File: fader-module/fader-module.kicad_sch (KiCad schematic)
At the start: 26 parts, among them IC1 LMD18245T_NOPB, J4 Conn_01x05_Pin, J5 Conn_01x05_Pin, SW1 1825910-6, SW2 1825910-6, U5 ATMEGA328P-AUR

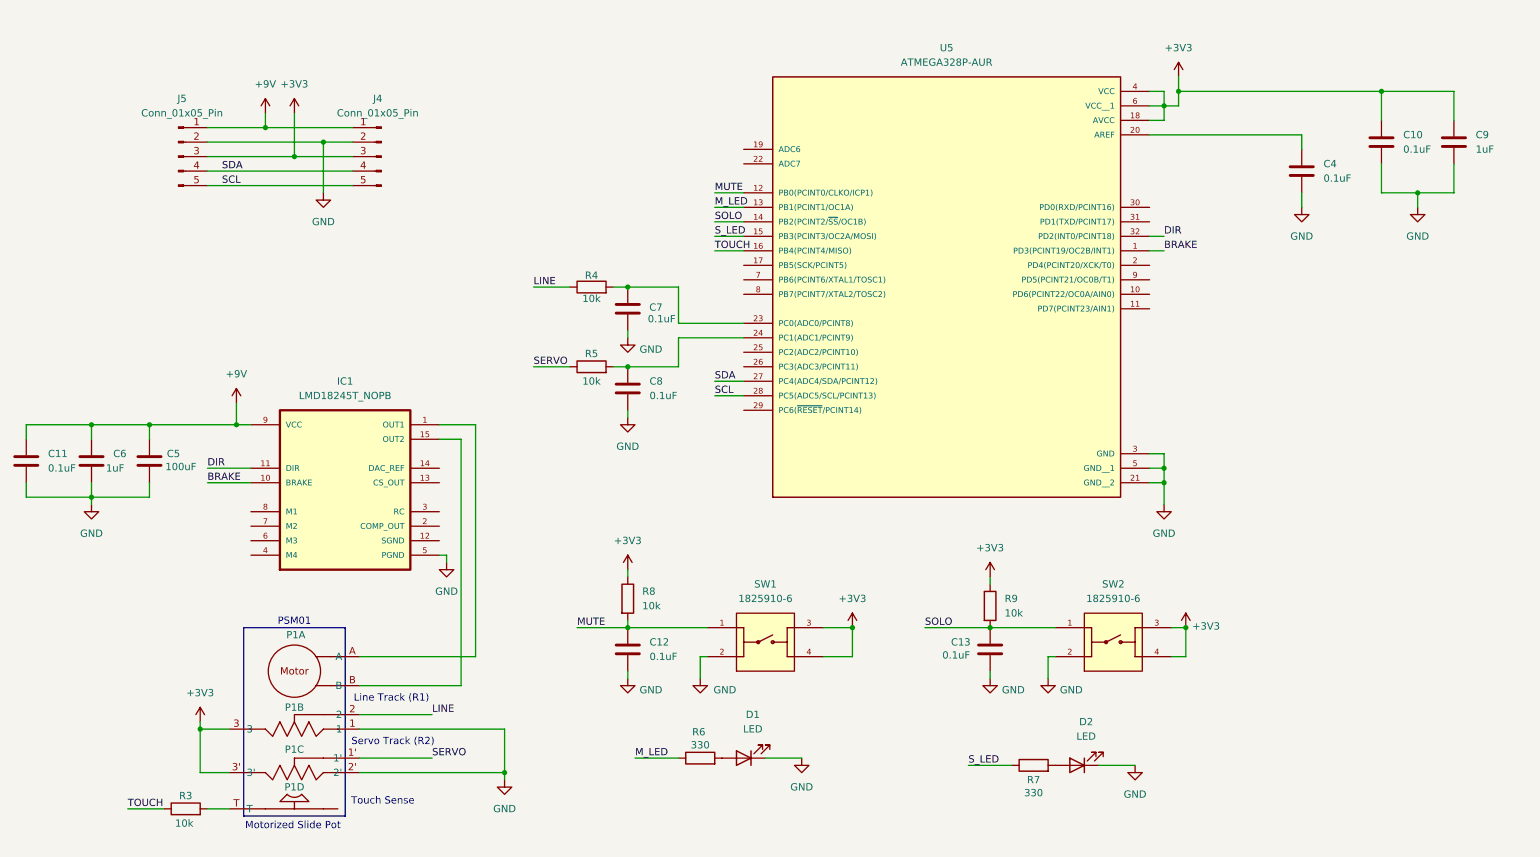
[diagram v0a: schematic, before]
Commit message: move fader module to new project
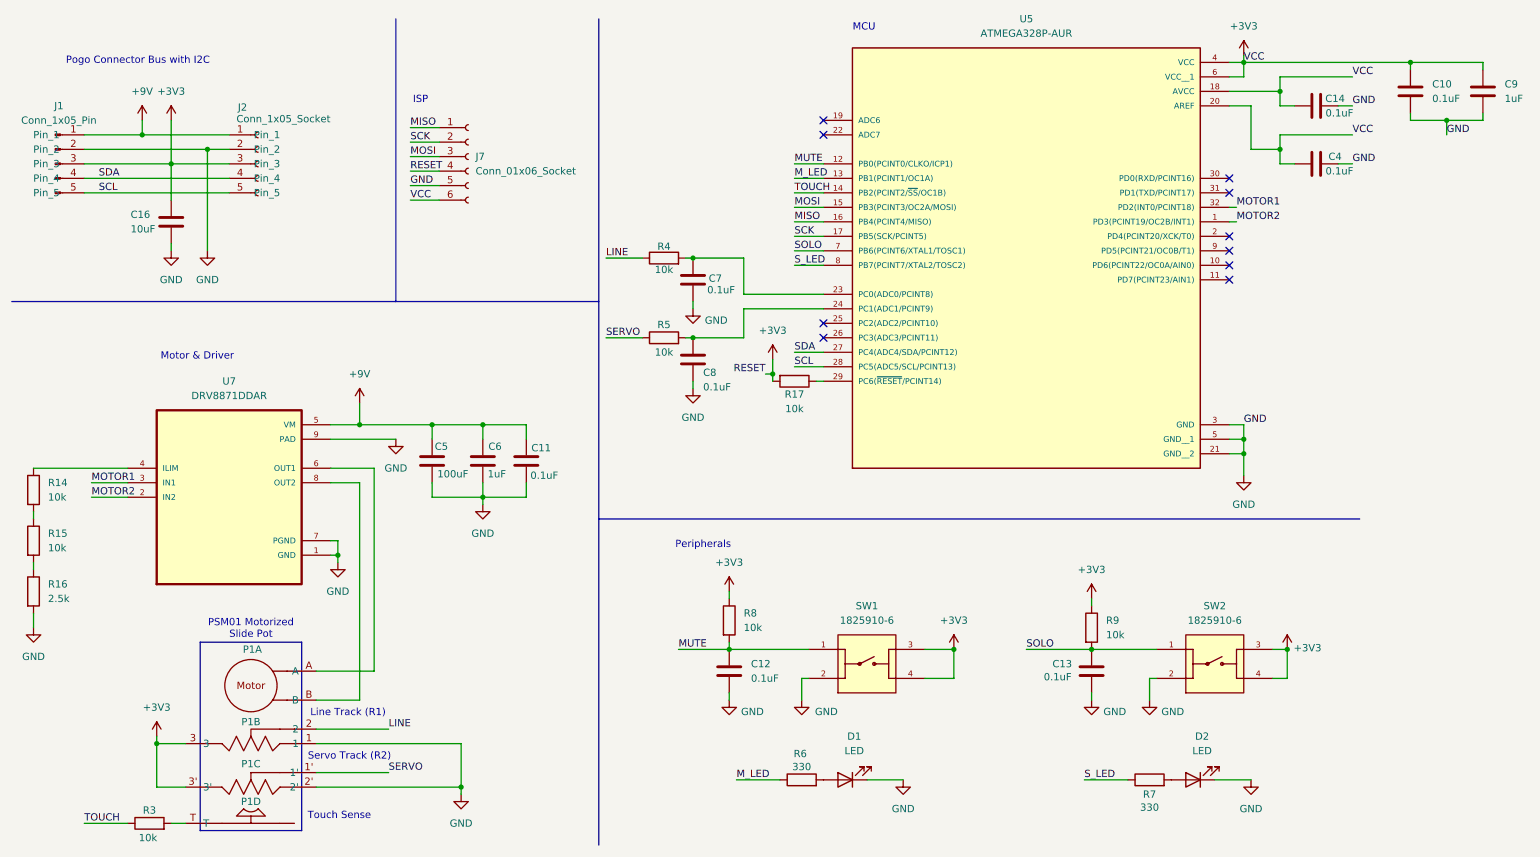
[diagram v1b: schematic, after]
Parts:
- removed IC1: LMD18245T_NOPB, LMD18245T_NOPB:TO-220-15, symbol LMD18245T/NOPB-ND:LMD18245T_NOPB
- removed J4, J5: Conn_01x05_Pin, symbol Connector:Conn_01x05_Pin
- added C14: 0.1uF, Capacitor_SMD:C_0805_2012Metric_Pad1.18x1.45mm_HandSolder, symbol Device:C
- added C16: 10uF, Capacitor_SMD:C_0805_2012Metric_Pad1.18x1.45mm_HandSolder, symbol Device:C
- added J1: Conn_1x05_Pin, MG05254:MG05254-M-RA-1N1S, symbol MG05254:Conn_MG05254_1x05_Pin
- added J2: Conn_1x05_Socket, MG05254:MG05254-M-RA-1N1S, symbol MG05254:Conn_MG05254_1x05_Socket
- added J7: Conn_01x06_Socket, Connector_IDC:IDC-Header_2x03_P2.54mm_Vertical, symbol Connector:Conn_01x06_Socket
- added R14, R15, R17: 10k, Resistor_SMD:R_0805_2012Metric_Pad1.20x1.40mm_HandSolder, symbol Device:R
- added R16: 2.5k, Resistor_SMD:R_0805_2012Metric_Pad1.20x1.40mm_HandSolder, symbol Device:R
- added U7: DRV8871DDAR, DRV8871DDAR:VREG_LM5017MR_NOPB, symbol DRV8871DDAR:DRV8871DDAR
- C10, C11, C12, C13, C4, C6, C7, C8, C9: footprint (none) -> Capacitor_SMD:C_0805_2012Metric_Pad1.18x1.45mm_HandSolder
- C5, R6: footprint (none) -> Capacitor_SMD:C_1206_3216Metric_Pad1.33x1.80mm_HandSolder
- D1, D2: footprint (none) -> LED_SMD:LED_0805_2012Metric_Pad1.15x1.40mm_HandSolder
- P1: footprint (none) -> PSM01:PSM01-081A_BRN
- R3, R4, R5, R7, R8, R9: footprint (none) -> Resistor_SMD:R_0805_2012Metric_Pad1.20x1.40mm_HandSolder
- SW1, SW2: footprint 1825910-6:SW_1825910-6-4 -> 1825910_6:SW_1825910-6-4
- U5: footprint ATMEGA328P-AUR:QFP80P900X900X120-32N -> ATMEGA328P_AUR:QFP80P900X900X120-32N
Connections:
- net +3V3: now also C4.1, U5.20 (AREF), C14.1, C16.1, J1.3 (Pin_3), J2.3 (Pin_3), J7.4 (Pin_4), J7.6 (Pin_6), R17.2
- net +9V: now also J1.1 (Pin_1), J2.1 (Pin_1), U7.5 (VM)
- net GND: now also C14.2, C16.2, J1.2 (Pin_2), J2.2 (Pin_2), J7.5 (Pin_5), R16.2, U7.1 (GND), U7.7 (PGND), U7.9 (PAD)
- net SCL: now also J1.5 (Pin_5), J2.5 (Pin_5)
- net SDA: now also J1.4 (Pin_4), J2.4 (Pin_4)
- net SOLO: now also U5.7 (PB6(PCINT6/XTAL1/TOSC1)); no longer U5.14 (PB2(PCINT2/~{SS}/OC1B))
- net S_LED: now also U5.8 (PB7(PCINT7/XTAL2/TOSC2)); no longer U5.15 (PB3(PCINT3/OC2A/MOSI))
- net TOUCH: now also U5.14 (PB2(PCINT2/~{SS}/OC1B)); no longer U5.16 (PB4(PCINT4/MISO))
- net SCK: now reaches U5.17 (PB5(SCK/PCINT5))
- net SCK: now also J7.2 (Pin_2)
- net at U5.29 (PC6(~{RESET}/PCINT14)): now also R17.1
- net at P1.A: now also U7.6 (OUT1)
- net at P1.B: now also U7.8 (OUT2)
- net BRAKE renamed MOTOR2
- net MOTOR2: now also U7.2 (IN2)
- net DIR renamed MOTOR1
- net MOTOR1: now also U7.3 (IN1)
- new net: R15.2, R16.1
- new net: R14.1, U7.4 (ILIM)
- new net: R14.2, R15.1
- new net MISO: J7.1 (Pin_1), U5.16 (PB4(PCINT4/MISO))
- new net MOSI: J7.3 (Pin_3), U5.15 (PB3(PCINT3/OC2A/MOSI))
- no-connect marks 0 -> 10
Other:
- note added: "ISP"
- note added: "MCU"
- note added: "Motor & Driver"
- note added: "PSM01 Motorized Slide Pot"
- note added: "Peripherals"
- note added: "Pogo Connector Bus with I2C"
- note removed: "Motorized Slide Pot"
- note removed: "PSM01"
- moved on the sheet: C10, C11, C12, C13, C5, C6, C7, C8, C9, D1, D2, P1A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

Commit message: i will combust
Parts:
- removed J7: Conn_01x06_Socket, Connector_IDC:IDC-Header_2x03_P2.54mm_Vertical, symbol Connector:Conn_01x06_Socket
- removed P1: ~, PSM01:PSM01-081A_BRN, symbol PSM01:PSM01
- added J3: Conn_01x02_Pin, TerminalBlock_Phoenix:TerminalBlock_Phoenix_MKDS-1,5-2-5.08_1x02_P5.08mm_Horizontal, symbol Connector:Conn_01x02_Pin
- added J4, J6: Conn_01x06_Pin, Connector_IDC:IDC-Header_2x03_P2.54mm_Vertical, symbol Connector:Conn_01x06_Pin
- D1, D2: footprint LED_SMD:LED_0805_2012Metric_Pad1.15x1.40mm_HandSolder -> Connector_Molex:Molex_KK-254_AE-6410-02A_1x02_P2.54mm_Vertical
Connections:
- net +3V3: now also J4.1 (Pin_1), J6.4 (Pin_4), J6.6 (Pin_6)
- net GND: now also J4.2 (Pin_2), J6.5 (Pin_5)
- net LINE: now also J4.3 (Pin_3)
- net MISO: now also J6.1 (Pin_1)
- net MOSI: now also J6.3 (Pin_3)
- net SCK: now also J6.2 (Pin_2)
- net SERVO: now also J4.4 (Pin_4)
- net TOUCH: now also J4.5 (Pin_5); no longer U5.14 (PB2(PCINT2/~{SS}/OC1B))
- net A: now reaches U7.6 (OUT1)
- net A: now also J3.1 (Pin_1)
- net B: now reaches U7.8 (OUT2)
- net B: now also J3.2 (Pin_2)
- net at R3.2: now also U5.14 (PB2(PCINT2/~{SS}/OC1B))
- no-connect marks 10 -> 11
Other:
- note added: "Ext to Motor Terminals"
- note added: "Motor Driver"
- note added: "To PSM01 Motorized Slide Pot (Externally Wired)"
- note removed: "Motor & Driver"
- note removed: "PSM01 Motorized Slide Pot"
- moved on the sheet: C11, C5, C6, R14, R15, R16, R3, U7

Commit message: the fuckin u7 clearance is acting up again
i also forgot how to wire a button LOL
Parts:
- removed C13: 0.1uF, Capacitor_SMD:C_0805_2012Metric_Pad1.18x1.45mm_HandSolder, symbol Device:C
- added C1: 1uF, Capacitor_SMD:C_0805_2012Metric_Pad1.18x1.45mm_HandSolder, symbol Device:C
- added H1, H2, H3, H4: MountingHole, MountingHole:MountingHole_3.2mm_M3, symbol Mechanical:MountingHole
- added R1, R2: 10k, Resistor_SMD:R_0805_2012Metric_Pad1.20x1.40mm_HandSolder, symbol Device:R
- C12: value 0.1uF -> 1uF
- R6: value 330 -> 1k; footprint Capacitor_SMD:C_1206_3216Metric_Pad1.33x1.80mm_HandSolder -> Resistor_SMD:R_0805_2012Metric_Pad1.20x1.40mm_HandSolder
- R7: value 330 -> 1k
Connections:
- net +3V3: now also R2.1; no longer R9.1, SW1.3, SW1.4, SW2.3, SW2.4
- net GND: now also SW1.3, SW1.4, SW2.3, SW2.4, C1.2; no longer SW1.2, SW2.2
- net MUTE: now also R1.1; no longer SW1.1
- net SOLO: now also R9.1, C1.1, R2.2; no longer R9.2, SW2.1
- new net: R1.2, SW1.1, SW1.2
- new net: R9.2, SW2.1, SW2.2
